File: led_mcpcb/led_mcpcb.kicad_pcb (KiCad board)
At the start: 2 copper layers, 100 x 100 mm, 109 parts, among them U1 TMP112xxDRL

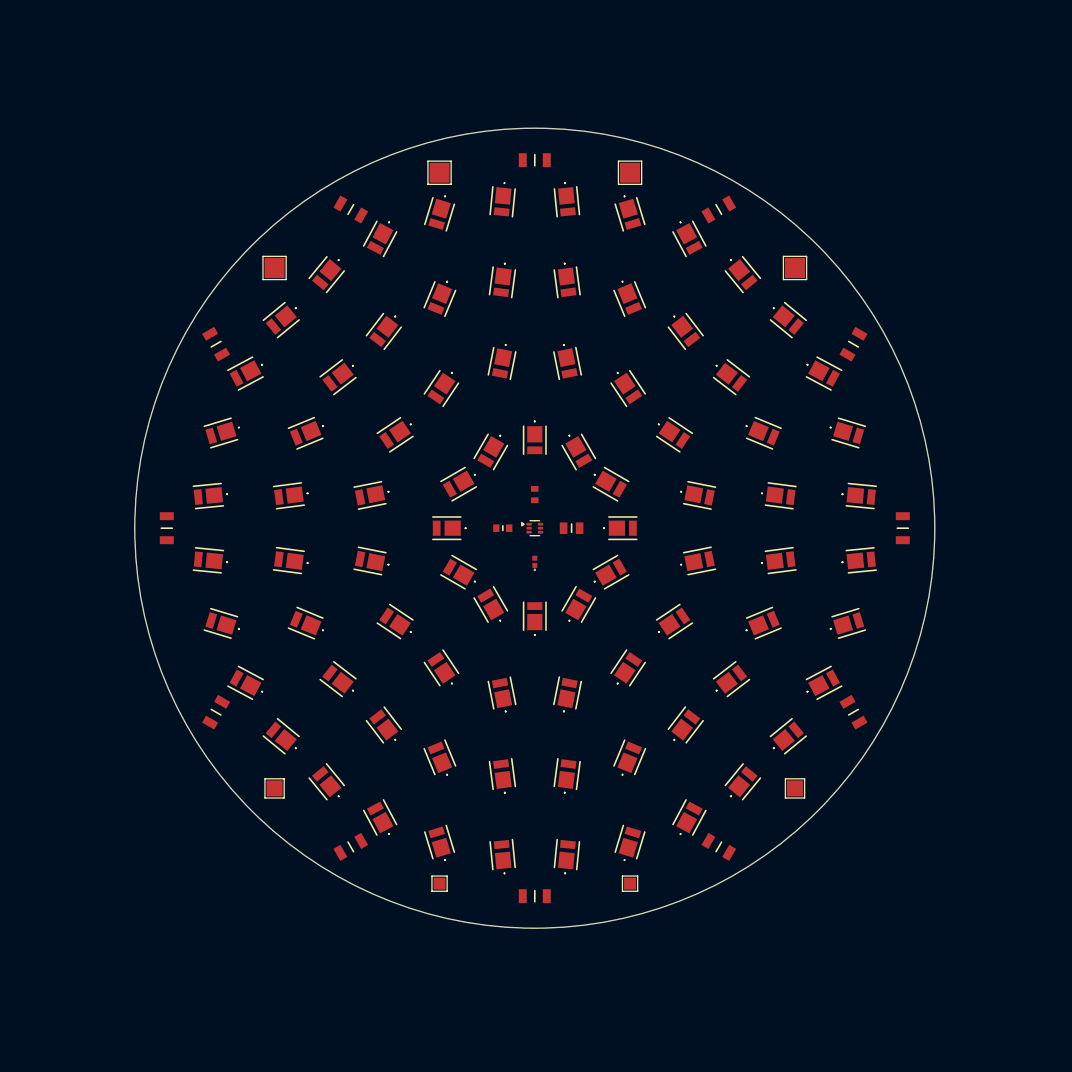
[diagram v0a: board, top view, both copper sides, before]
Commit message: Finalize KiCad PCB sources for 5-piece test build
Commit the completed Open Vettam 15CCT KiCad source design files prepared for the initial five-piece production test run.

Included files are limited to the schematic hierarchy, PCB layouts, KiCad project files, and the LED MCPCB design-rules file. Generated BOM exports, fabrication output archives, freerouting/temp files, logs, backups, images, netlists, and Altium import artifacts are intentionally left unstaged.

Updated main controller board sources:

- open_vettam_15CCT.kicad_sch

- open_vettam_15CCT.kicad_pcb

- open_vettam_15CCT.kicad_pro

- 24v_Input.kicad_sch

- 24-5_buck.kicad_sch

- MCU.kicad_sch

- cc_driver.kicad_sch

Updated LED MCPCB sources:

- led_mcpcb/led_mcpcb.kicad_sch

- led_mcpcb/led_mcpcb.kicad_pcb

- led_mcpcb/led_mcpcb.kicad_pro

- led_mcpcb/led_mcpcb.kicad_dru

- led_mcpcb/CW-5000.kicad_sch

- led_mcpcb/WW-3000.kicad_sch

- led_mcpcb/digital_temp.kicad_sch
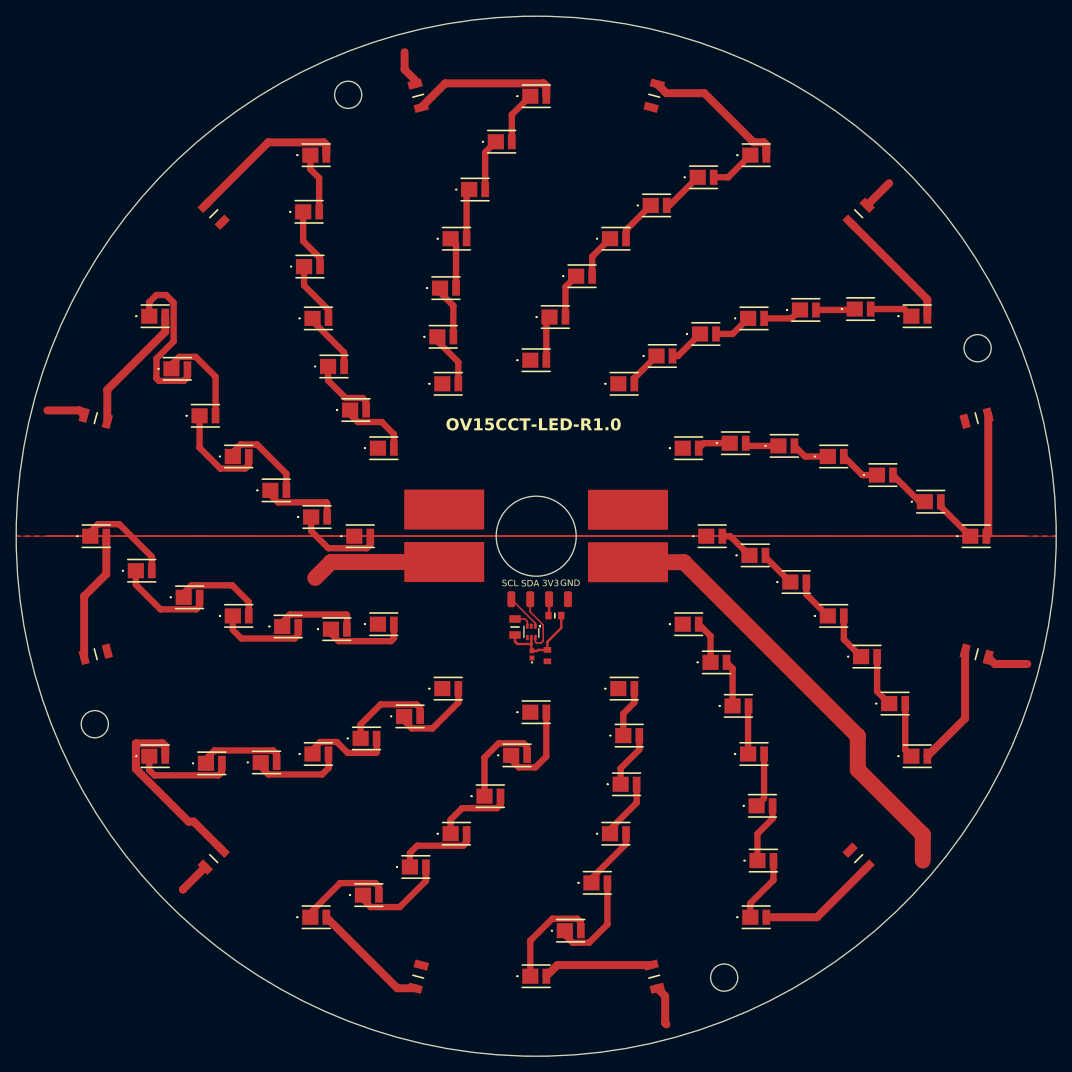
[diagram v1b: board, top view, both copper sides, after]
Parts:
- removed CW+, CW-, WW+, WW-: PAD, TestPoint_Pad_2.5x2.5mm
- removed R15, R16: 6.8Ω 1%, RESC3116X65N
- removed TEMP_3V3, TEMP_GND: PAD, TestPoint_Pad_2.0x2.0mm
- removed TEMP_SCL, TEMP_SDA: PAD, TestPoint_Pad_1.5x1.5mm
- added 3V3: TEMP_3V3, Connector_Wire:SolderWirePad_1x01_SMD_1x2mm, F.Cu at (150.5, 109.1)
- added GND: TEMP_GND, Connector_Wire:SolderWirePad_1x01_SMD_1x2mm, F.Cu at (152.9, 109.1)
- added J1: CW+, Connector_Wire:SolderWirePad_1x01_SMD_5x10mm, F.Cu at (160.4, 104.5)
- added J2: CW-, Connector_Wire:SolderWirePad_1x01_SMD_5x10mm, F.Cu at (160.4, 98.0)
- added J3: WW+, Connector_Wire:SolderWirePad_1x01_SMD_5x10mm, F.Cu at (137.4, 104.5)
- added J4: WW-, Connector_Wire:SolderWirePad_1x01_SMD_5x10mm, F.Cu at (137.4, 97.9)
- added R2: 6.8Ω 1%, SamacSys_Parts:RESC3116X65N, F.Cu at (163.7, 156.3)
- added R4: 6.8Ω 1%, SamacSys_Parts:RESC3116X65N, F.Cu at (93.9, 86.5)
- added SCL: TEMP_SCL, Connector_Wire:SolderWirePad_1x01_SMD_1x2mm, F.Cu at (145.8, 109.1)
- added SDA: TEMP_SDA, Connector_Wire:SolderWirePad_1x01_SMD_1x2mm, F.Cu at (148.2, 109.1)
- C1: footprint CAPC1608X90N -> SamacSys_Parts:CAPC1608X90N
- C2: footprint C0402 -> SamacSys_Parts:C0402
- LED1, LED10, LED11, LED12, LED13, LED14, LED15, LED16, LED17, LED18, LED19, LED2, LED20, LED21, LED22, LED23, LED24, LED3, LED4, LED43, LED44, LED45, LED46, LED47, LED48, LED5, LED59, LED6, LED60, LED62, LED7, LED71, LED72, LED73, LED74, LED75, LED76, LED77, LED78, LED79, LED8, LED80, LED81, LED82, LED83, LED84, LED9: footprint L1283090HA35000K1 -> SamacSys_Parts:L1283090HA35000K1
- LED25, LED26, LED27, LED28, LED29, LED30, LED31, LED32, LED33, LED34, LED36, LED37, LED38, LED39, LED40, LED42: value WW3000K -> CW5000K; footprint L1283090HA35000K1 -> SamacSys_Parts:L1283090HA35000K1
- LED35, LED41: value WW3000K -> CW5000K; footprint L1285090HA35000K1 -> SamacSys_Parts:L1283090HA35000K1
- LED49, LED50, LED51, LED52, LED53, LED55, LED56, LED57, LED58, LED63, LED64, LED65, LED66, LED67, LED68, LED69, LED70: value CW5000K -> WW3000K; footprint L1283090HA35000K1 -> SamacSys_Parts:L1283090HA35000K1
- LED54: value CW5000K -> WW3000K; footprint L1283090HA35000K1 -> SamacSys_Parts:L1285090HA35000K1
- LED61: footprint L1283090HA35000K1 -> SamacSys_Parts:L1285090HA35000K1
- R1: value 1K 1% -> 6.8Ω 1%; footprint RESC1608X55N -> SamacSys_Parts:RESC3116X65N
- R10, R11, R12, R5, R6, R7, R8, R9: footprint RESC3116X65N -> SamacSys_Parts:RESC3116X65N
- R13: value 6.8Ω 1% -> 1K 1%; footprint RESC3116X65N -> SamacSys_Parts:RESC1608X55N
- R14: value 6.8Ω 1% -> 5K 5%; footprint RESC3116X65N -> SamacSys_Parts:RESC2012X50N
- R3: value 5K 5% -> 6.8Ω 1%; footprint RESC2012X50N -> SamacSys_Parts:RESC3116X65N
- U1: footprint SOT-563 -> Package_TO_SOT_SMD:SOT-563
- moved R6 94.4 mm to (189.2, 60.9), turned to 45 degrees
- moved R5 94.3 mm to (134.2, 46.2), turned to 105 degrees
- moved LED62 86.4 mm to (99.6, 105.6), turned to 0 degrees
- moved LED61 84.1 mm to (105.6, 108.9), turned to 0 degrees
- moved R8 83.0 mm to (134.2, 156.3), turned to 75 degrees
- moved R9 82.6 mm to (93.9, 116.0), turned to 15 degrees
- moved R7 82.4 mm to (189.2, 141.6), turned to 135 degrees
- moved LED76 82.2 mm to (169.8, 56.4), turned to 0 degrees
- moved R10 81.6 mm to (108.6, 60.9), turned to -45 degrees
- moved LED75 81.3 mm to (164.0, 59.9), turned to 0 degrees
- moved LED42 81.2 mm to (196.6, 73.7), turned to 0 degrees
- moved LED77 80.7 mm to (176.4, 53.6), turned to 0 degrees
- moved LED70 80.4 mm to (121.4, 53.6), turned to 0 degrees
- moved LED74 78.1 mm to (158.9, 64.1), turned to 0 degrees
- moved LED49 73.8 mm to (176.4, 148.9), turned to 0 degrees
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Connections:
- LED13 pad 1: GND -> Net-(LED12-A)
- LED14 pad 2: Net-(LED14-A) -> CW_STR2
- LED15 pad 1: Net-(LED14-A) -> GND
- LED19 pad 1: GND -> Net-(LED18-A)
- LED21 pad 2: Net-(LED21-A) -> CW_STR3
- LED22 pad 1: Net-(LED21-A) -> GND
- LED25 pad 1: GND -> Net-(LED24-A)
- LED28 pad 2: Net-(LED28-A) -> CW_STR4
- LED29 pad 1: Net-(LED28-A) -> GND
- LED31 pad 1: GND -> Net-(LED30-A)
- LED35 pad 2: Net-(LED35-A) -> CW_STR5
- LED36 pad 1: Net-(LED35-A) -> GND
- LED37 pad 1: GND -> Net-(LED36-A)
- LED42 pad 2: Net-(LED42-A) -> CW_STR6
- LED49 pad 1: GND -> Net-(LED48-A)
- LED49 pad 2: Net-(LED49-A) -> WW_STR1
- LED50 pad 1: Net-(LED49-A) -> GND
- LED55 pad 1: Net-(LED55-K) -> Net-(LED54-A)
- LED55 pad 2: CW_STR1 -> Net-(LED55-A)
- LED56 pad 1: Net-(LED12-A) -> Net-(LED55-A)
- LED56 pad 2: CW_STR2 -> WW_STR2
- LED57 pad 1: Net-(LED18-A) -> GND
- LED57 pad 2: CW_STR3 -> Net-(LED57-A)
- LED58 pad 1: Net-(LED24-A) -> Net-(LED57-A)
- LED58 pad 2: CW_STR4 -> Net-(LED58-A)
- LED59 pad 1: Net-(LED30-A) -> Net-(LED58-A)
- LED59 pad 2: WW_STR1 -> Net-(LED59-A)
- LED6 pad 2: Net-(LED55-K) -> Net-(LED6-A)
- LED60 pad 1: Net-(LED36-A) -> Net-(LED59-A)
- LED60 pad 2: WW_STR2 -> Net-(LED60-A)
- LED61 pad 1: Net-(LED42-A) -> Net-(LED60-A)
- LED61 pad 2: WW_STR3 -> Net-(LED61-A)
- LED62 pad 1: Net-(LED48-A) -> Net-(LED61-A)
- LED62 pad 2: WW_STR4 -> Net-(LED62-A)
- LED63 pad 1: Net-(LED54-A) -> Net-(LED62-A)
- LED63 pad 2: CW_STR5 -> WW_STR3
- LED7 pad 1: GND -> Net-(LED6-A)
- LED7 pad 2: Net-(LED7-A) -> CW_STR1
- LED70 pad 2: CW_STR6 -> WW_STR4
- LED8 pad 1: Net-(LED7-A) -> GND
- R1 pad 1: Net-(U1-V+) -> CW_STR1
- R1 pad 2: 3V3 -> Net-(J1-Pin_1)
- R10 pad 1: WW_STR6 -> WW_STR4
- R10 pad 2: vcc -> Net-(J3-Pin_1)
- R11 pad 1: CW_STR1 -> WW_STR5
- R11 pad 2: vcc -> Net-(J3-Pin_1)
- R12 pad 1: CW_STR2 -> WW_STR6
- R12 pad 2: vcc -> Net-(J3-Pin_1)
- R13 pad 1: CW_STR3 -> Net-(U1-V+)
- R13 pad 2: vcc -> 3V3
- R14 pad 1: CW_STR4 -> Net-(U1-ALERT)
- R14 pad 2: vcc -> Net-(U1-V+)
- R3 pad 1: Net-(U1-ALERT) -> CW_STR3
- R3 pad 2: Net-(U1-V+) -> Net-(J1-Pin_1)
- R5 pad 1: WW_STR1 -> CW_STR5
- R5 pad 2: vcc -> Net-(J1-Pin_1)
- R6 pad 1: WW_STR2 -> CW_STR6
- R6 pad 2: vcc -> Net-(J1-Pin_1)
- R7 pad 1: WW_STR3 -> WW_STR1
- R7 pad 2: vcc -> Net-(J3-Pin_1)
- R8 pad 1: WW_STR4 -> WW_STR2
- R8 pad 2: vcc -> Net-(J3-Pin_1)
- R9 pad 1: WW_STR5 -> WW_STR3
- R9 pad 2: vcc -> Net-(J3-Pin_1)
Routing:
- net Net-(J1-Pin_1): track 0.00 -> 84.1 mm
- net CW_STR3: track 0.00 -> 23.3 mm
- net Net-(LED27-A): track 0.00 -> 21.2 mm
- net WW_STR4: track 0.00 -> 19.8 mm
- net CW_STR5: track 0.00 -> 18.3 mm
- net WW_STR5: track 0.00 -> 18.0 mm
- net Net-(J3-Pin_1): track 0.00 -> 17.0 mm
- net WW_STR3: track 0.00 -> 16.3 mm
- net CW_STR4: track 0.00 -> 16.1 mm
- net CW_STR6: track 0.00 -> 15.7 mm
- net WW_STR6: track 0.00 -> 15.2 mm
- net WW_STR1: track 0.00 -> 15.2 mm
- net CW_STR1: track 0.00 -> 15.1 mm
- net WW_STR2: track 0.00 -> 14.8 mm
- net CW_STR2: track 0.00 -> 13.7 mm
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- added copper zone on F.Cu, net GND
- added copper zone on F.Cu, net Net-(J1-Pin_1)
- added copper zone on F.Cu, net Net-(J3-Pin_1)
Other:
- board size 100 x 100 mm -> 130 x 130 mm
- board text added: "OV15CCT-LED-R1.0"
- board text removed: "Single-side Al MCPCB, 100mm OD"
